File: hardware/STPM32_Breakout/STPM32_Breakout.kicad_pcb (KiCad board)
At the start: 2 copper layers, 38.2 x 28 mm, 34 parts, among them J1 BREADBOARD I/O, SW1 RESET, U1 STPM32, Y1 16MHz

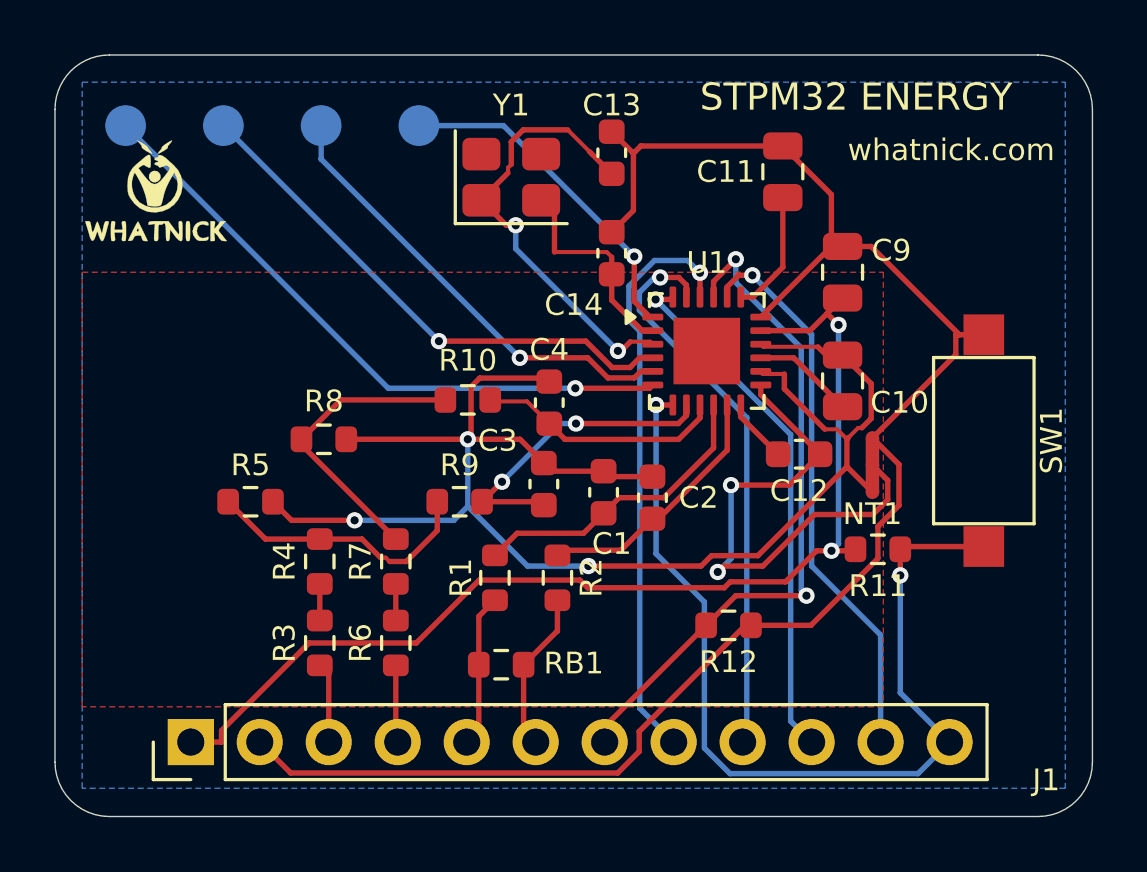
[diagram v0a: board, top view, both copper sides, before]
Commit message: Refine STPM32 silkscreen placement
Co-authored-by: Copilot <223556219+Copilot@users.noreply.github.com>
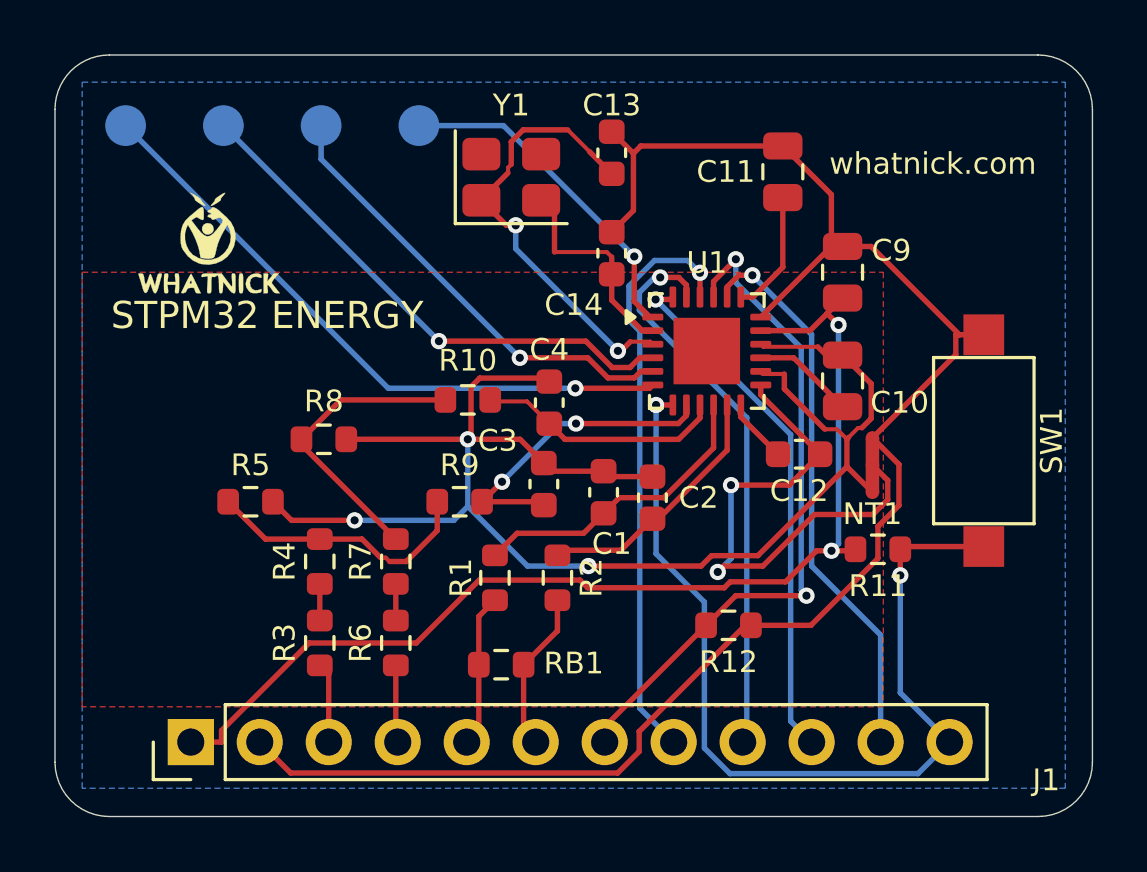
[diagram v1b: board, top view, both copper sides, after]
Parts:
- moved LOGO_OSHW 4.45 mm to (51.1, 27.9)
- moved LOGO_W 2.74 mm to (25.7, 26.9)
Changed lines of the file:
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@@
 	(footprint "Whatnick_Logo"
 		(layer "F.Cu")
-		(at 23.7 25)
+		(at 25.654 26.924)
 		(property "Reference" "LOGO_W"
 			(at 0 0 180)
@@
 	(footprint "OSHW_Logo"
 		(layer "B.Cu")
-		(at 54.4 25 180)
+		(at 51.054 27.94 180)
 		(descr "Open Source Hardware Symbol")
 		(tags "Logo Symbol OSHW")
@@
 	)
 	(gr_text "whatnick.com"
-		(at 53 23.5 0)
+		(at 52.324 24.003 0)
 		(layer "F.SilkS")
 		(effects
@@
 	)
 	(gr_text "STPM32 ENERGY"
-		(at 49.5 21.55 0)
+		(at 27.813 29.591 0)
 		(layer "F.SilkS")
 		(effects
@@
 	)
 	(gr_text "TAPR OHL 1.0"
-		(at 25.2 31 0)
+		(at 26.289 32.004 0)
 		(layer "B.SilkS")
 		(effects
@@
 	)
 	(gr_text "NOT FOR DIRECT MAINS"
-		(at 42 21.2 0)
+		(at 43.434 22.098 0)
 		(layer "B.SilkS")
 		(effects
